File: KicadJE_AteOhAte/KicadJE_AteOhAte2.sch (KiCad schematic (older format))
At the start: 34 parts, among them J201 In_Accent, J202 In Gate, J203 Out Final, P201 Doepfer_Power_10pin, Q201 MMBT2222A, SW201 In or cascade, SW202 Out 1, SW203 In or cascade, SW204 Out 2 FB, SW205 HI/LO, U201 TL072, U202 TL072

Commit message: PCB init shape
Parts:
- removed C201, C204: 100uF 16v, Capacitor_THT:CP_Radial_D5.0mm_P2.50mm, symbol Device:CP
- removed SW203: In or cascade, AJ-Dropbox-Kicad:SP1MS1, symbol Switch:SW_SPDT
- removed SW204: Out 2 FB, AJ-Dropbox-Kicad:SP1MS1, symbol Switch:SW_SPDT
- removed SW205: HI/LO, AJ-Dropbox-Kicad:SP1MS1, symbol Switch:SW_SPDT
- added C?: 10n, Capacitor_SMD:C_0805_2012Metric_Pad1.15x1.40mm_HandSolder, symbol Device:C
- added D?: 1N1007, Diode_SMD:D_SOD-123, symbol Device:D
- added R?: 4k7, Resistor_SMD:R_0805_2012Metric_Pad1.15x1.40mm_HandSolder, symbol Device:R
- added R? (x5): 100k, Resistor_SMD:R_0805_2012Metric_Pad1.15x1.40mm_HandSolder, symbol Device:R
- added R?: 47k, Resistor_SMD:R_0805_2012Metric_Pad1.15x1.40mm_HandSolder, symbol Device:R
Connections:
- net labels added: +12V, -12V
- wire segments 81 -> 107
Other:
- moved on the sheet: Q201, SW201, U202B

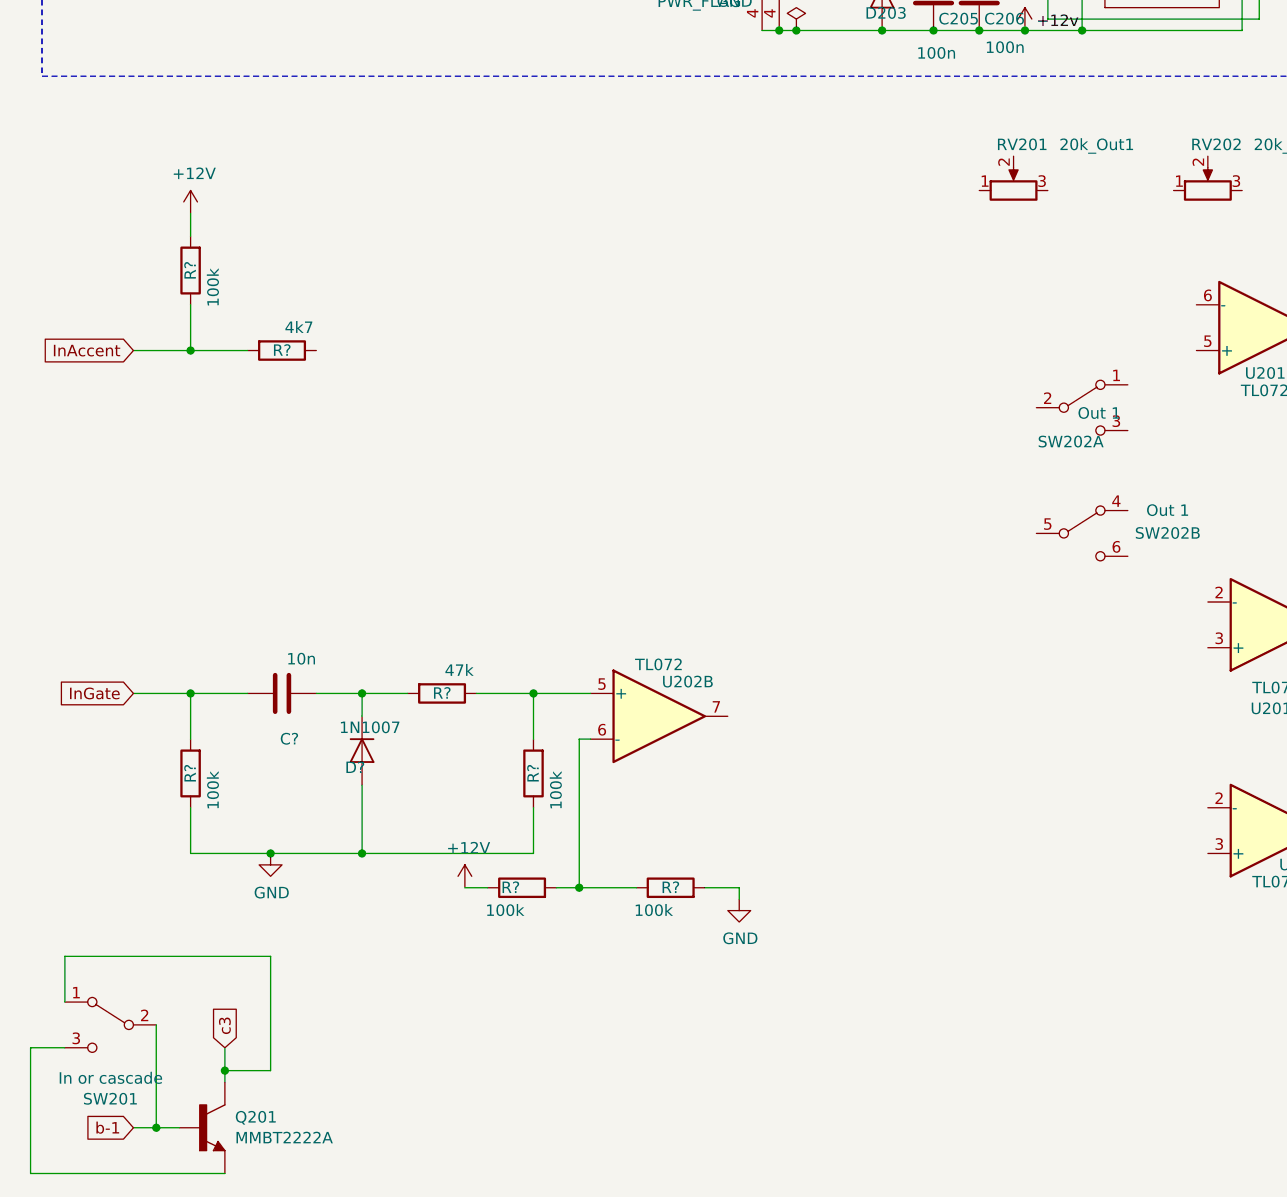
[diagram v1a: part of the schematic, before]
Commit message: ACC and Trig input done sch
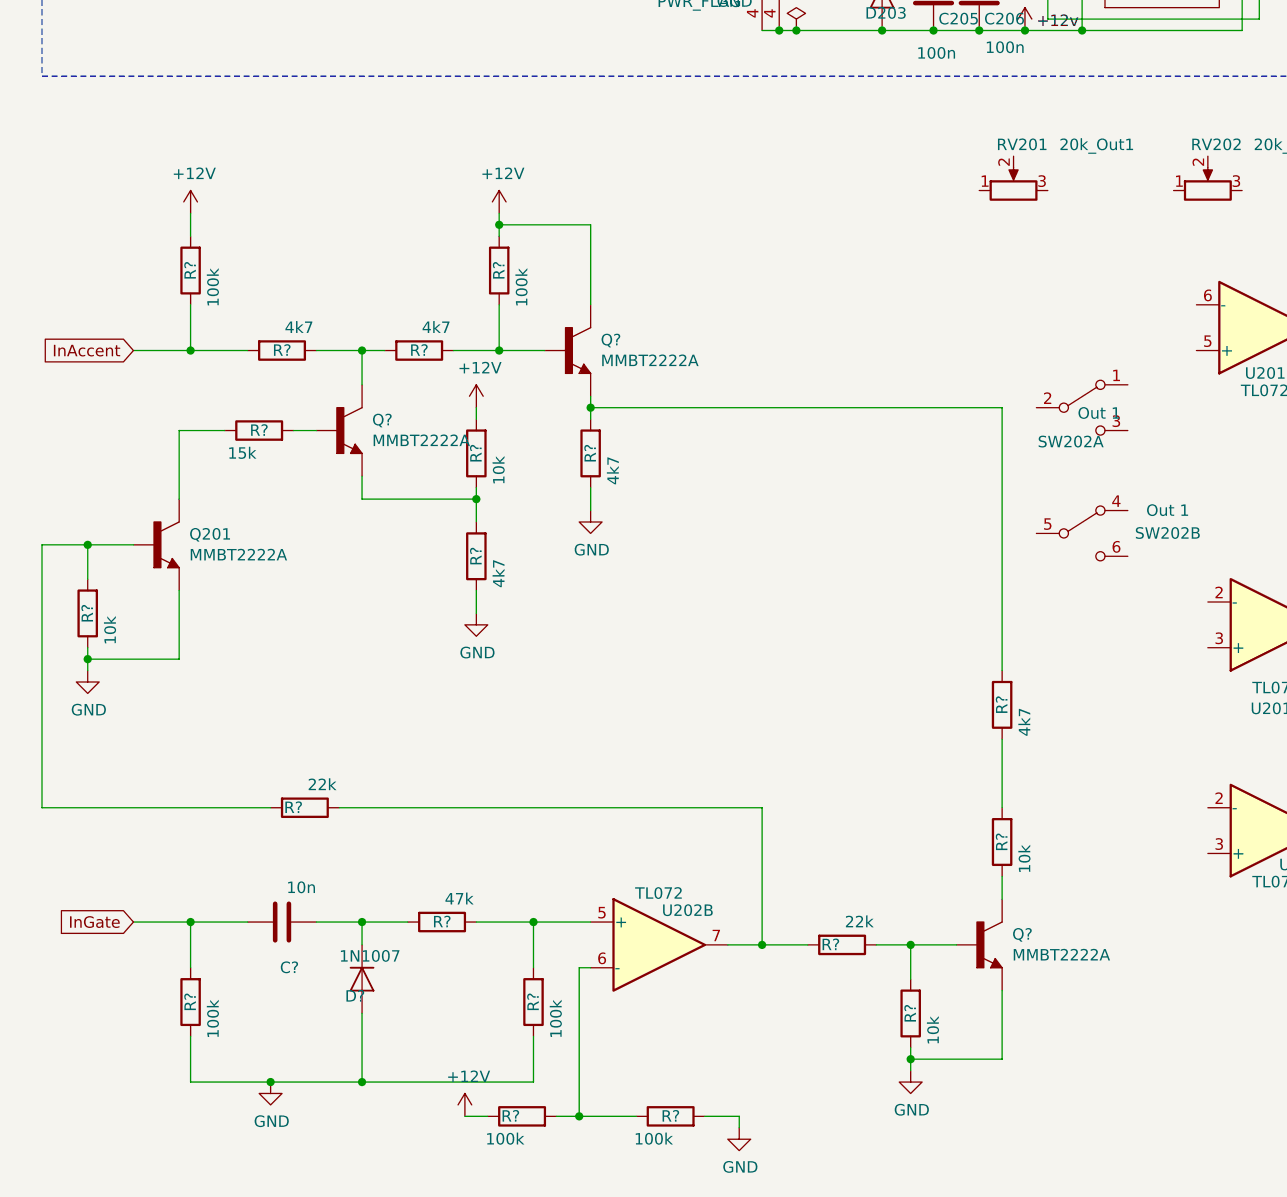
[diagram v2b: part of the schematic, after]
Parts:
- removed SW201: In or cascade, AJ-Dropbox-Kicad:SP1MS1, symbol Switch:SW_SPDT
- added Q? (x3): MMBT2222A, Package_TO_SOT_SMD:SOT-23_Handsoldering, symbol MMBT2222A:MMBT2222A
- added R? (x4): 4k7, Resistor_SMD:R_0805_2012Metric_Pad1.15x1.40mm_HandSolder, symbol Device:R
- added R?: 100k, Resistor_SMD:R_0805_2012Metric_Pad1.15x1.40mm_HandSolder, symbol Device:R
- added R? (x4): 10k, Resistor_SMD:R_0805_2012Metric_Pad1.15x1.40mm_HandSolder, symbol Device:R
- added R?: 15k, Resistor_SMD:R_0805_2012Metric_Pad1.15x1.40mm_HandSolder, symbol Device:R
- added R? (x2): 22k, Resistor_SMD:R_0805_2012Metric_Pad1.15x1.40mm_HandSolder, symbol Device:R
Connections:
- net +12V: now also Q?.3 (C), R?.2, R?.2
- net GND: now also Q201.2 (E), Q?.2 (E), R?.1, R?.1, R?.1, R?.1
- net at U202.7: now also R?.1, R?.2
- net at R?.1: now also Q?.3 (C), R?.2
- net b-1: no longer names the net of Q201.1 (B)
- net b-1: now also R?.2, R?.2
- net c3: no longer names the net of Q201.3 (C)
- net c3: now also R?.1
- new net: Q?.1 (B), R?.1, R?.1
- new net: Q?.1 (B), R?.2
- new net: Q?.2 (E), R?.1, R?.2
- new net: Q?.2 (E), R?.2, R?.2
- new net: Q?.1 (B), R?.1, R?.2
- new net: Q?.3 (C), R?.1
- new net: R?.1, R?.2
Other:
- moved on the sheet: C?, D?, Q201, R?, U202B

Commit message: 2nd stage Tom sch initiated
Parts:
- added C?: C4, Capacitor_SMD:C_0805_2012Metric_Pad1.15x1.40mm_HandSolder, symbol Device:C
- added C?: C6, Capacitor_SMD:C_0805_2012Metric_Pad1.15x1.40mm_HandSolder, symbol Device:C
- added C?: C8, Capacitor_SMD:C_0805_2012Metric_Pad1.15x1.40mm_HandSolder, symbol Device:C
- added D?: 1N4148, Diode_SMD:D_SOD-123, symbol Device:D
- added Q?: MMBT2907A, symbol MMBT2907A:MMBT2907A
- added Q?: MMBT2222A, Package_TO_SOT_SMD:SOT-23_Handsoldering, symbol MMBT2222A:MMBT2222A
- added R? (x3): 4k7, Resistor_SMD:R_0805_2012Metric_Pad1.15x1.40mm_HandSolder, symbol Device:R
- added R?: 2M2, Resistor_SMD:R_0805_2012Metric_Pad1.15x1.40mm_HandSolder, symbol Device:R
- added R?: 33k, Resistor_SMD:R_0805_2012Metric_Pad1.15x1.40mm_HandSolder, symbol Device:R
- D205: renamed from D?; value 1N1007 -> 1N4148
- gave numbers to parts that had none: 23
- renumbered C202 to C201, C203 to C202, C205 to C203, C206 to C204, Q201 to Q203, R205 to R207, SW202 to SW201
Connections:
- net GND: now also C?.2, Q?.2 (E), R?.1
- net at Q201.2 (E), R212.2, R215.2: now also Q?.E
- net at R215.1, R217.2: now also Q?.B
- new net: C?.2, Q?.C, R?.2, R?.2
- new net: D?.2 (A), R?.1
- new net: C?.1, D?.1 (K), R?.1
- new net: R?.1, R?.2
- new net: Q?.1 (B), R?.2
- new net: C?.2, Q?.3 (C), R?.1
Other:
- moved on the sheet: RV201, RV202, RV203, SW201A, SW201B, U201A, U201B, U202A

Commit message: 2nd
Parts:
- added C?: C9, Capacitor_SMD:C_0805_2012Metric_Pad1.15x1.40mm_HandSolder, symbol Device:C
- added C?: C10, Capacitor_SMD:C_0805_2012Metric_Pad1.15x1.40mm_HandSolder, symbol Device:C
- added D?: 1N4148, Diode_SMD:D_SOD-123, symbol Device:D
- added R?: 22k, Resistor_SMD:R_0805_2012Metric_Pad1.15x1.40mm_HandSolder, symbol Device:R
- added R?: R17, Resistor_SMD:R_0805_2012Metric_Pad1.15x1.40mm_HandSolder, symbol Device:R
- added R?: R18, Resistor_SMD:R_0805_2012Metric_Pad1.15x1.40mm_HandSolder, symbol Device:R
- added R?: 820k, Resistor_SMD:R_0805_2012Metric_Pad1.15x1.40mm_HandSolder, symbol Device:R
- added R?: 33k, Resistor_SMD:R_0805_2012Metric_Pad1.15x1.40mm_HandSolder, symbol Device:R
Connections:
- net +12V: now also R?.2
- net GND: now also SW201.1 (A), U201.5 (+), D?.2 (A), R?.1
- net at U201.6 (-): now also R?.2
- net at U201.1: now also C?.2, R?.1, R?.1
- net at U201.2 (-): now also C?.1, R?.2
- net at U201.3 (+): now also R?.1, R?.2, R?.2
- net at SW201.2 (B): now also R?.1
- net at C?.1: now also D?.1 (K), R?.2
- new net: C?.1, C?.2
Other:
- moved on the sheet: RV201, RV202, SW201A, SW201B, U201A, U201B

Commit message: Initial SCH for the Tom
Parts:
- added C?: C11, Capacitor_SMD:C_0805_2012Metric_Pad1.15x1.40mm_HandSolder, symbol Device:C
- added C?: C12, Capacitor_SMD:C_0805_2012Metric_Pad1.15x1.40mm_HandSolder, symbol Device:C
- added C?: 1n, Capacitor_SMD:C_0805_2012Metric_Pad1.15x1.40mm_HandSolder, symbol Device:C
- added C?: C7, Capacitor_SMD:C_0805_2012Metric_Pad1.15x1.40mm_HandSolder, symbol Device:C
- added D? (x2): 1N4148, Diode_SMD:D_SOD-123, symbol Device:D
- added R?: 33k, Resistor_SMD:R_0805_2012Metric_Pad1.15x1.40mm_HandSolder, symbol Device:R
- added R? (x2): 470k, Resistor_SMD:R_0805_2012Metric_Pad1.15x1.40mm_HandSolder, symbol Device:R
- added R? (x2): 1k, Resistor_SMD:R_0805_2012Metric_Pad1.15x1.40mm_HandSolder, symbol Device:R
- added R? (x2): 100k, Resistor_SMD:R_0805_2012Metric_Pad1.15x1.40mm_HandSolder, symbol Device:R
- added R?: 4k7, Resistor_SMD:R_0805_2012Metric_Pad1.15x1.40mm_HandSolder, symbol Device:R
- added R? (x2): 22k, Resistor_SMD:R_0805_2012Metric_Pad1.15x1.40mm_HandSolder, symbol Device:R
- J203: value Out Final -> Out Tom
- RV201: value 20k_Out1 -> 500k Tune
- RV202: value 20k_Out2 -> 100k Reverb
- RV203: value 20k_final -> 1M Decay
- SW201: value Out 1 -> Con/Tom
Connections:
- net GND: now also R?.2, RV201.3, RV202.1, C?.2, R?.1, R?.1; no longer R?.1
- net OutTom: now also R?.2
- net at U202.1: now also C?.2, R?.1, R?.1
- net at U202.2 (-): now also C?.1, C?.2, R?.2
- net at U202.3 (+): now also R?.2
- net at R?.2, U201.6 (-): now also R?.1
- net at U201.7: now also RV203.2, R?.1, R?.2
- net at RV203.3: now also R?.1
- net at RV201.1: now also D?.1 (K), D?.2 (A)
- net at RV201.2: now also R?.1
- net at C?.2, R?.1, R?.1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: now also C?.2
- net at R?.1, U201.3 (+): now also R?.1, R?.1; no longer R?.2, R?.2
- net at SW201.2 (B): now also R?.2; no longer R?.1
- net at SW201.4 (A): now also C?.1, C?.2, D?.1 (K), D?.2 (A), R?.2, R?.2
- net at SW201.5 (B): now also C?.1
- net at RV202.2: now also R?.2
- net at RV202.3: now also C?.1, R?.2
- net at C?.1: now also R?.1, R?.2
- new net: C?.1, R?.1, R?.2
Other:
- moved on the sheet: C201, C202, C203, C204, C205, C?, D201, D202, D203, D204, D205, D?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

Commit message: LT HT MT vals
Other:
- note added: "Tom LT MT HT\nC4 39n 33n 33n\nC6 47n 33n 27n\nC7 18n 15n 10n\nC8 6n8 2n7 2n7\nC9 56n 27n 27n\nC10 12n 12n 5n6\nC11 47n 27n 22n\nC12 47n 39n 33n\nR17 1k5 2k5 1k5\nR18 4k7 6k8 5k6"
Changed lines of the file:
@@
 Wire Notes Line
 	8850 550  4900 550
+Text Notes 9150 1650 0    50   ~ 0
+Tom LT      MT    HT\nC4    39n    33n    33n\nC6    47n    33n    27n\nC7    18n    15n    10n\nC8    6n8    2n7    2n7\nC9    56n    27n    27n\nC10  12n    12n    5n6\nC11  47n    27n    22n\nC12  47n    39n    33n\nR17  1k5    2k5    1k5\nR18  4k7    6k8    5k6
+Wire Notes Line
+	8950 550  10250 550
+Wire Notes Line
+	10250 550  10250 1850
+Wire Notes Line
+	10250 1850 8950 1850
+Wire Notes Line
+	8950 1850 8950 550
 $EndSCHEMATC

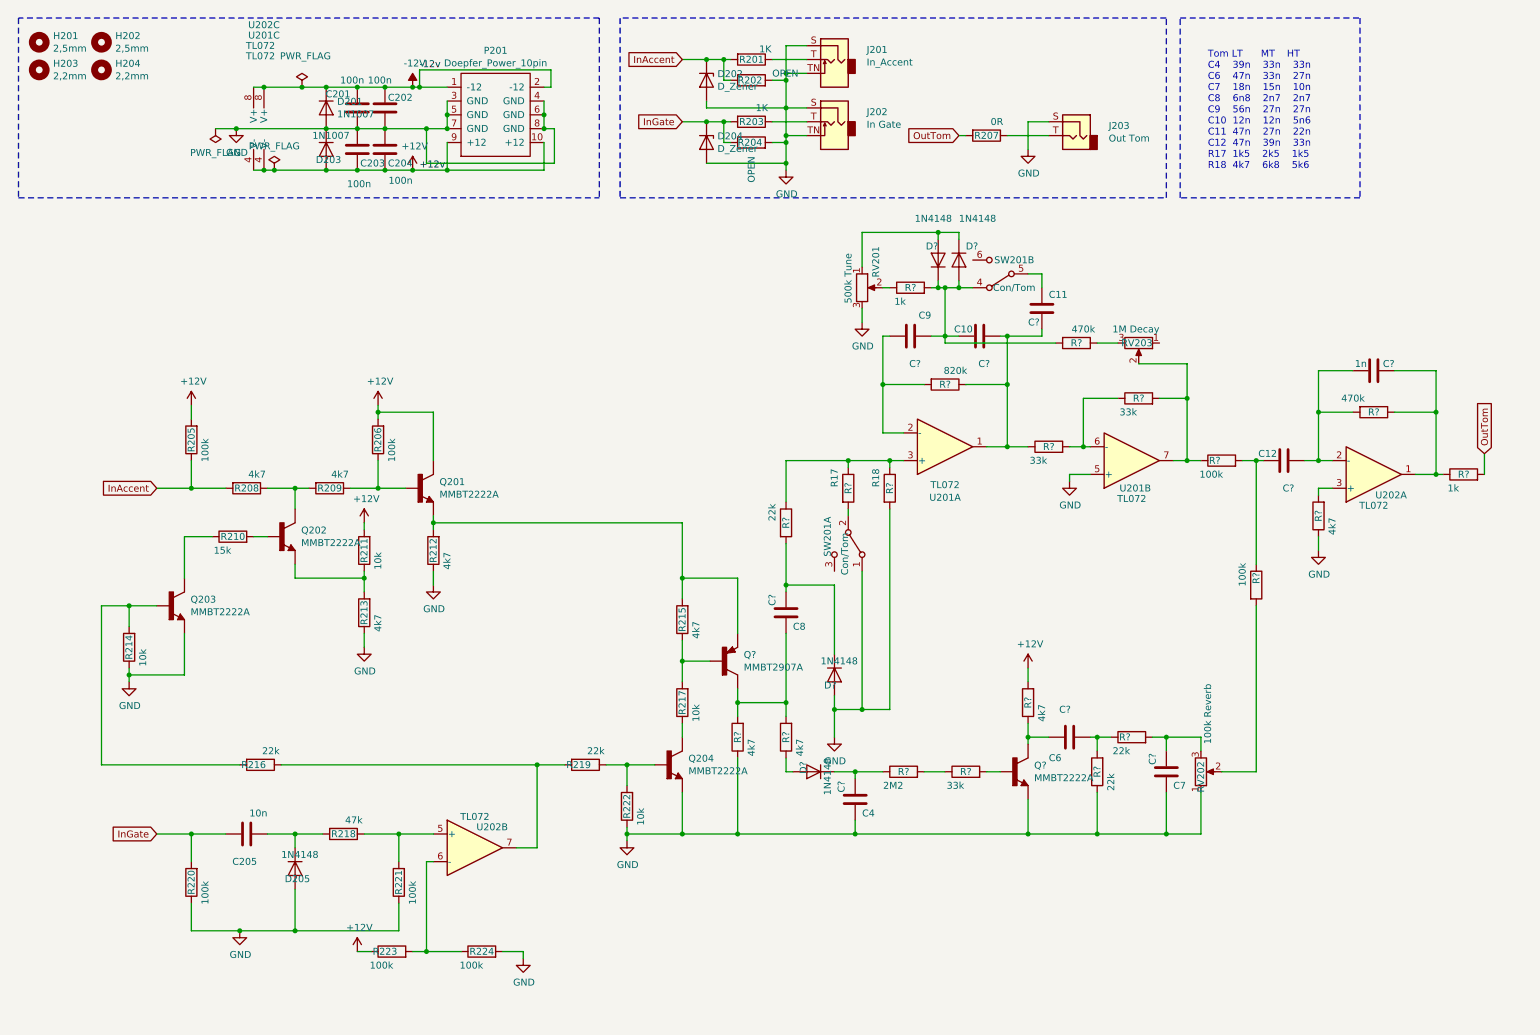
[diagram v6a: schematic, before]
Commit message: PCB footprint upd
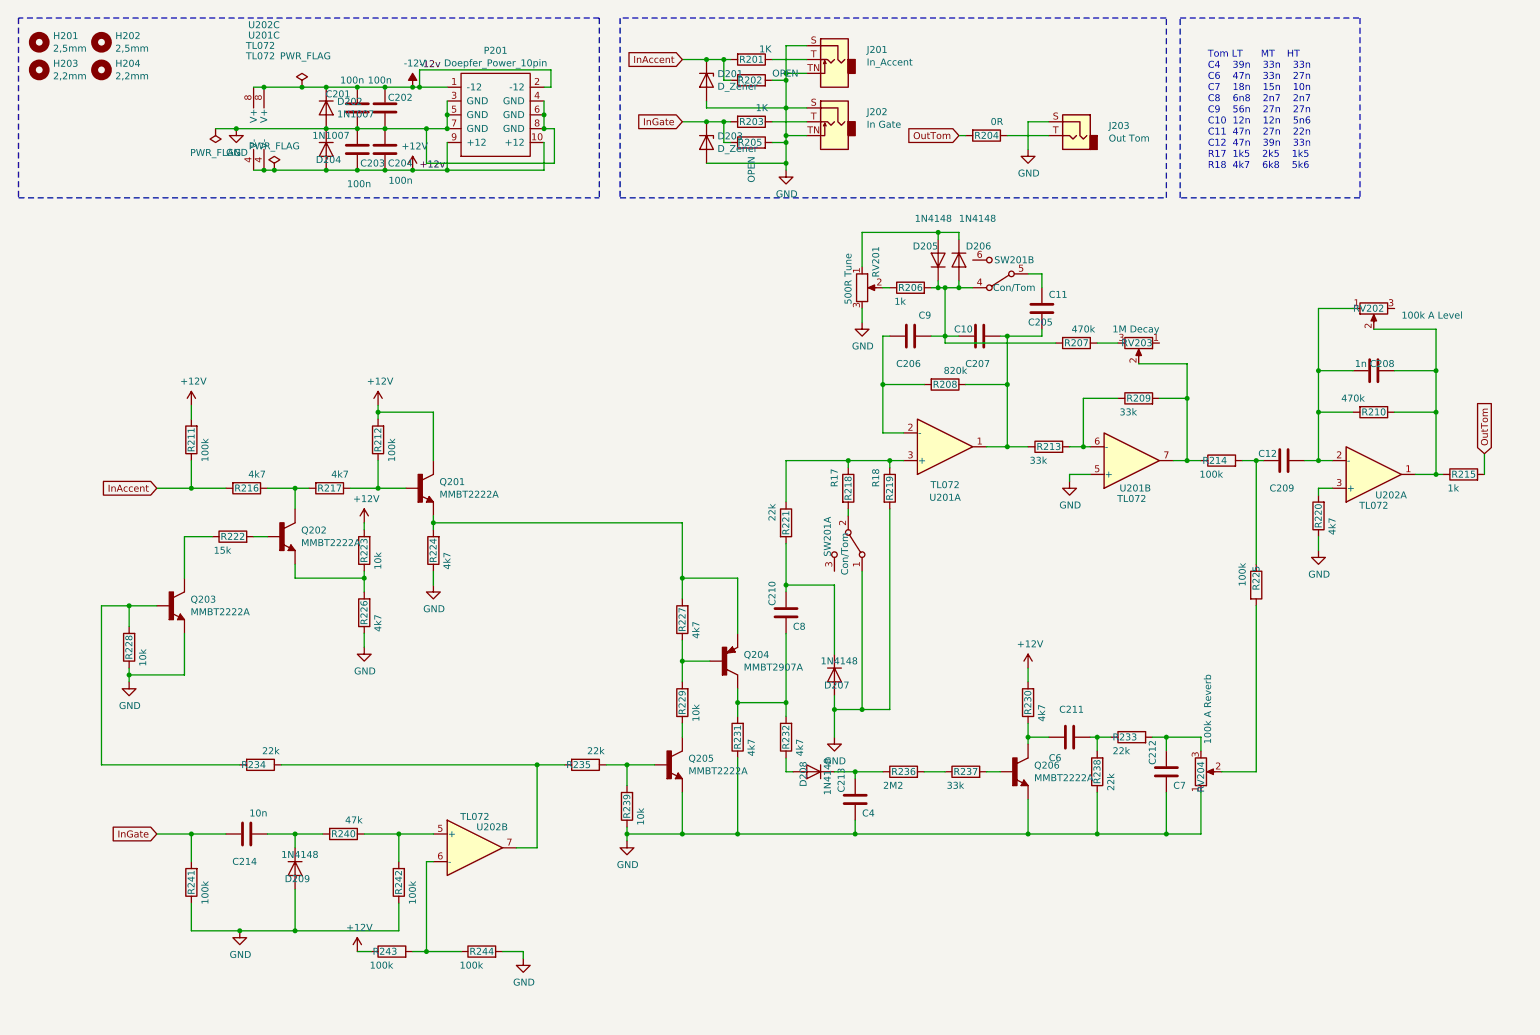
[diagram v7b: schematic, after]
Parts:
- added RV202: 100k A Level, Potentiometer_THT:Potentiometer_Piher_T-16H_Single_Horizontal, symbol Device:R_POT
- J202: footprint Connector_Audio:Jack_3.5mm_Ledino_KB3SPRS_Horizontal -> AJ-Dropbox-Kicad:PJ301SM
- Q204: renamed from Q?; footprint (none) -> Package_TO_SOT_SMD:SOT-23_Handsoldering
- RV201: value 500k Tune -> 500R Tune; footprint Potentiometer_THT:Potentiometer_China_RK09_Single_Vertical_AJ -> Potentiometer_THT:Potentiometer_Piher_T-16H_Single_Horizontal
- RV203: footprint Potentiometer_THT:Potentiometer_China_RK09_Single_Vertical_AJ -> Potentiometer_THT:Potentiometer_Piher_T-16H_Single_Horizontal
- RV204: renamed from RV202; value 100k Reverb -> 100k A Reverb; footprint Potentiometer_THT:Potentiometer_China_RK09_Single_Vertical_AJ -> Potentiometer_THT:Potentiometer_Piher_T-16H_Single_Horizontal
- gave numbers to parts that had none: 34
- renumbered C205 to C214, D202 to D201, D201 to D202, D204 to D203, D203 to D204, D205 to D209, Q204 to Q205, R207 to R204, R204 to R205, R205 to R211, R206 to R212, R208 to R216, R209 to R217, R210 to R222, R211 to R223, R212 to R224, R213 to R226, R215 to R227, R214 to R228, R217 to R229, R216 to R234, R219 to R235, R222 to R239, R218 to R240, R220 to R241, R221 to R242, R223 to R243, R224 to R244
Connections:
- net at C208.2, R210.1, R215.1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: now also RV202.2
- net at C208.1, C209.2, R210.2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: now also RV202.1
